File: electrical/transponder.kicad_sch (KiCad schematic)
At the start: 5 parts

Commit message: Upgraded G3X Touch to Axis
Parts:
- GDL52: value ~ -> (none)

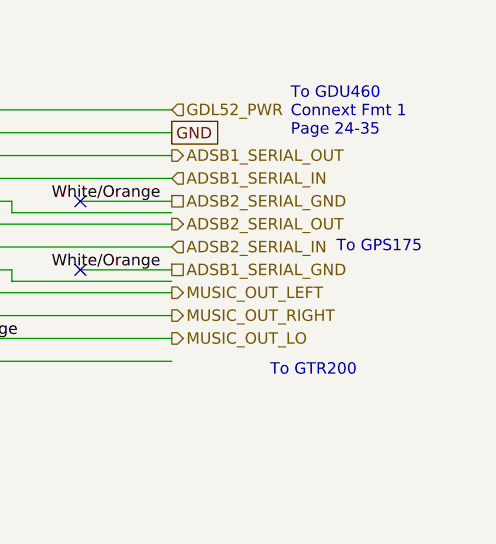
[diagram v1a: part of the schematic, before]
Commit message: Updated wiring to just do GDU Bat Lead leader. Also, keep pin 31 as effectively backup power like it was on G3X Touch
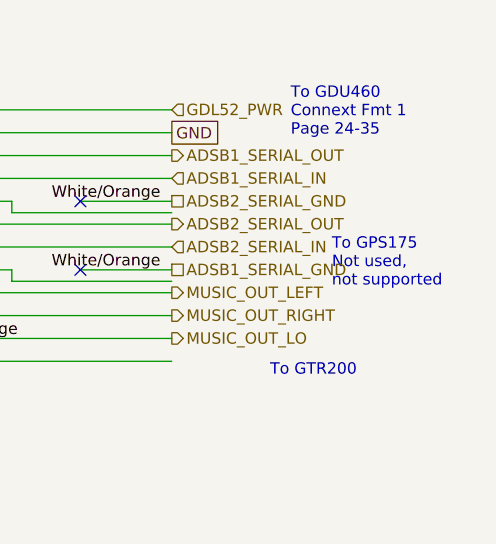
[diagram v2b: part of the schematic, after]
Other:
- note added: "To GPS175 Not used, not supported"
- note removed: "To GPS175"
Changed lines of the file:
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@@
 		(company "N877RV")
 	)
-	(text "To GPS175"
+	(text "To GPS175\nNot used,\nnot supported"
 		(exclude_from_sim no)
-		(at 258.318 40.132 0)
+		(at 257.81 43.942 0)
 		(effects
 			(font
